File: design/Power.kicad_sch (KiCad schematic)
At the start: 48 parts, among them U2 TC2117, U3 DRV8302

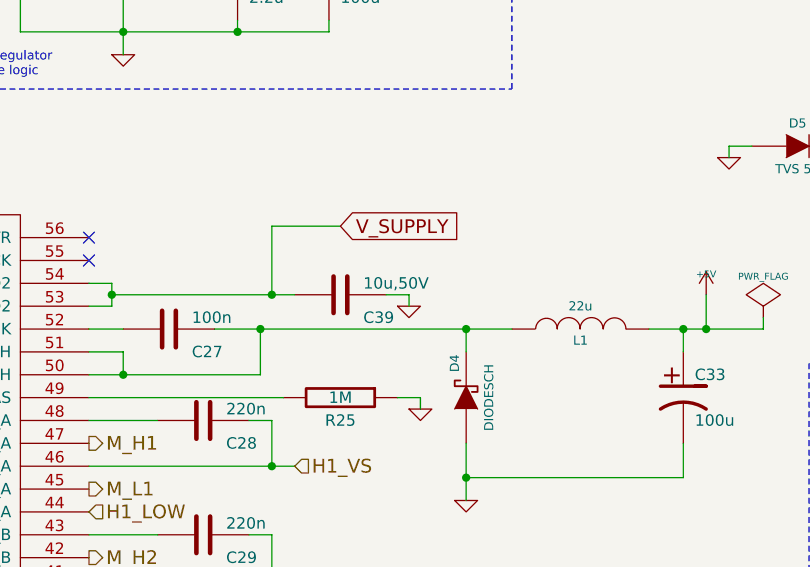
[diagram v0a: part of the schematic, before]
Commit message: extended board include input power caps and holes for wires
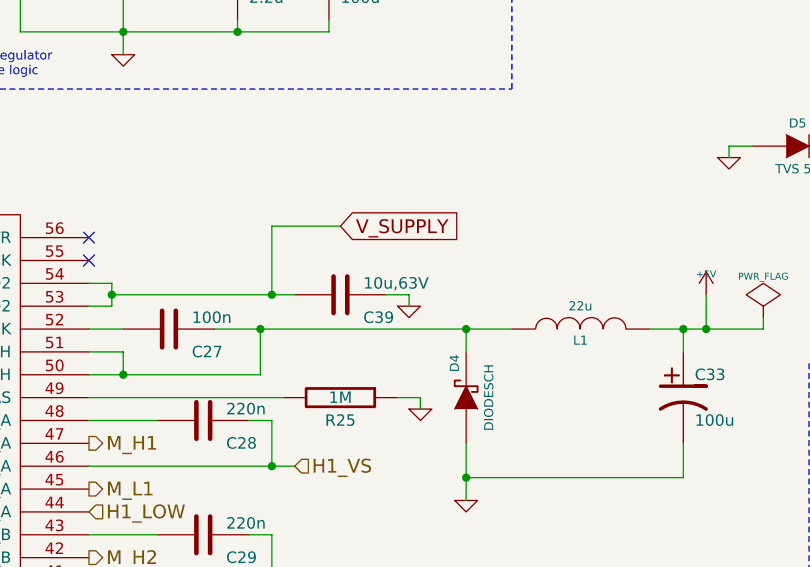
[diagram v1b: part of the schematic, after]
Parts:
- C39: value 10u,50V -> 10u,63V
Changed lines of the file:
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@@
 			)
 		)
-		(property "Value" "10u,50V"
+		(property "Value" "10u,63V"
 			(at 186.69 69.85 90)
 			(effects

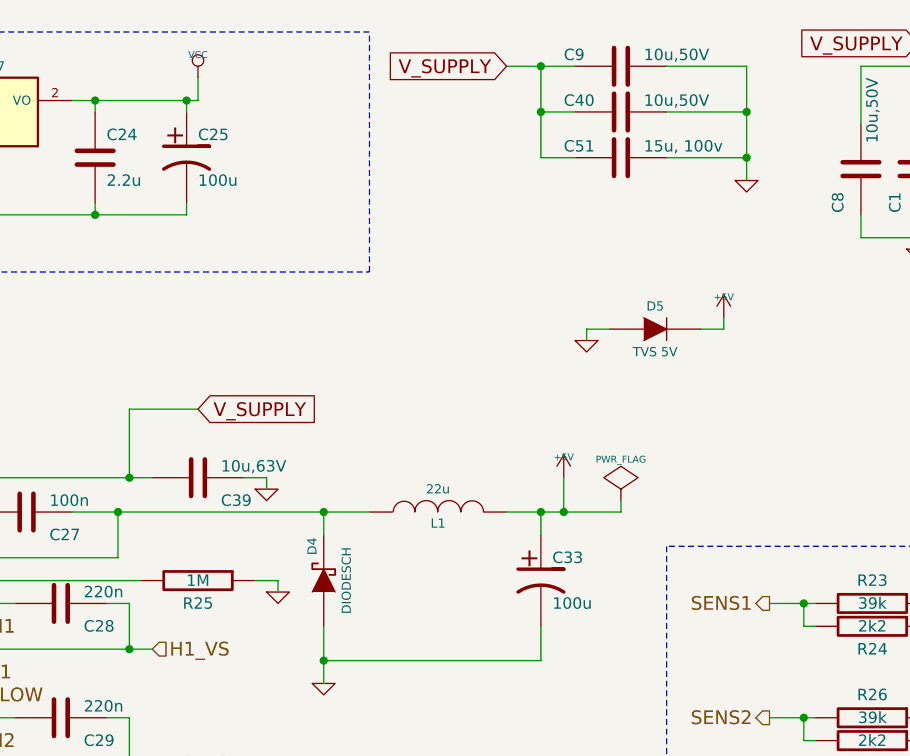
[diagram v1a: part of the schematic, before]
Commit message: v 4.13 produced by jlcpcb
Some serious issues with usb connectors facing the caps. Working fine
otherwise
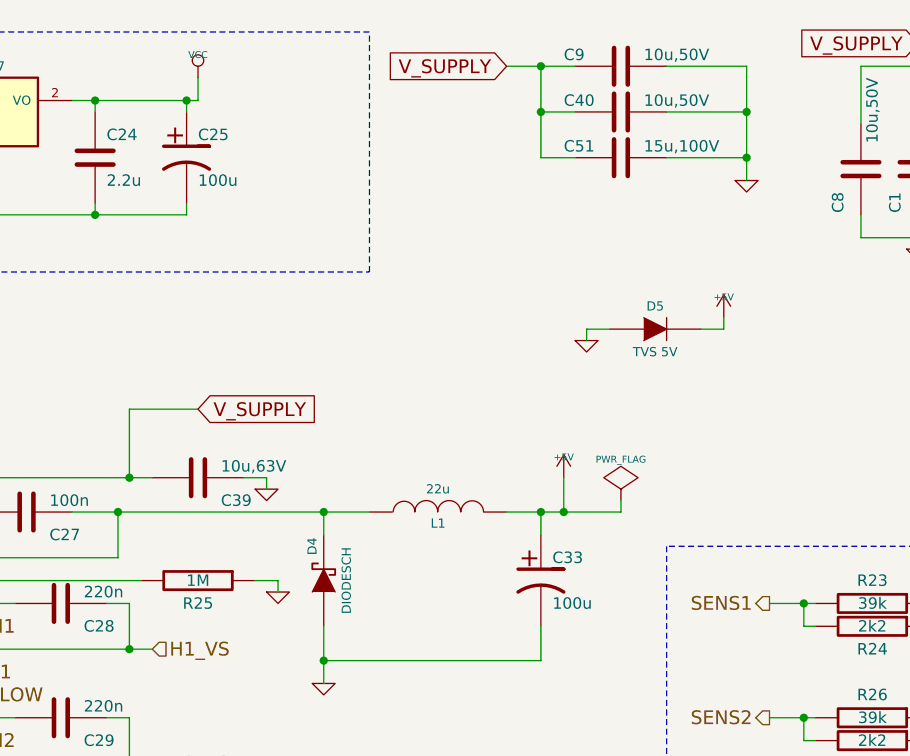
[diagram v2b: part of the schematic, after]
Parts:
- C1, C40, C43, C44, C49, C8, C9: JLCPCB (none) -> C13585
- C18, C20, C23, C24, C26, C52: JLCPCB (none) -> C23630
- C25, C33: JLCPCB (none) -> C116740
- C37: JLCPCB (none) -> C5795620
- C51: value 15u, 100v -> 15u,100V; JLCPCB (none) -> C5795620
- D4: JLCPCB (none) -> C6807782
- D5: JLCPCB (none) -> C2760868
- L1: JLCPCB (none) -> C139488
- U2: JLCPCB (none) -> C98655
- U3: JLCPCB (none) -> C79740

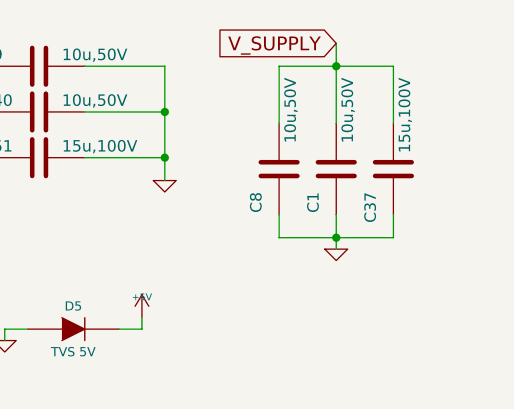
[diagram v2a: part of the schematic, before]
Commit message: v4.14 Changed power connectors to XT90 and XT60
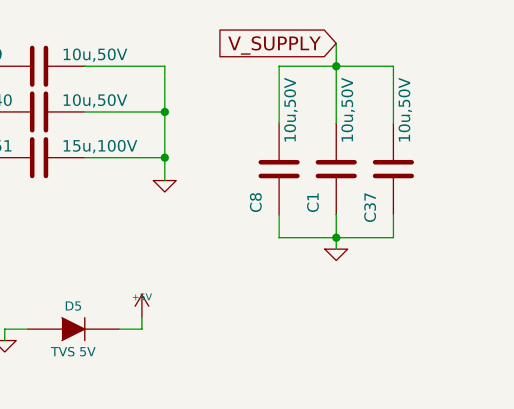
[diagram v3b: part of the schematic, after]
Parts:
- C37: value 15u,100V -> 10u,50V; footprint w_smd_cap:c_2220 -> CRF1:SMD-1206; JLCPCB C5795620 -> C13585
